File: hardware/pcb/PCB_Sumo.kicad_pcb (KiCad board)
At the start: 2 copper layers, 60 x 80 mm, 31 parts

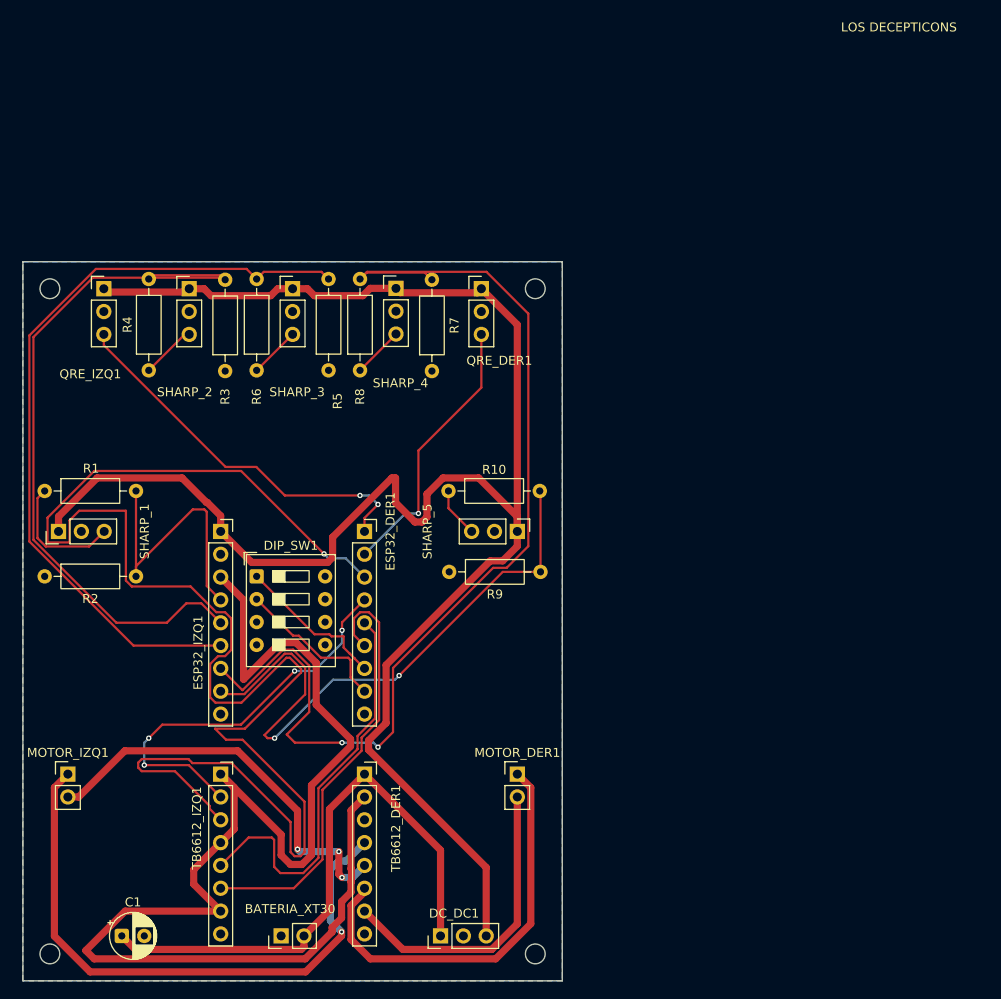
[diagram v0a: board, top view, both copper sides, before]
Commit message: PCB v2 (WIP): divisor de batería en GP6, ESP32 a 15.24 mm
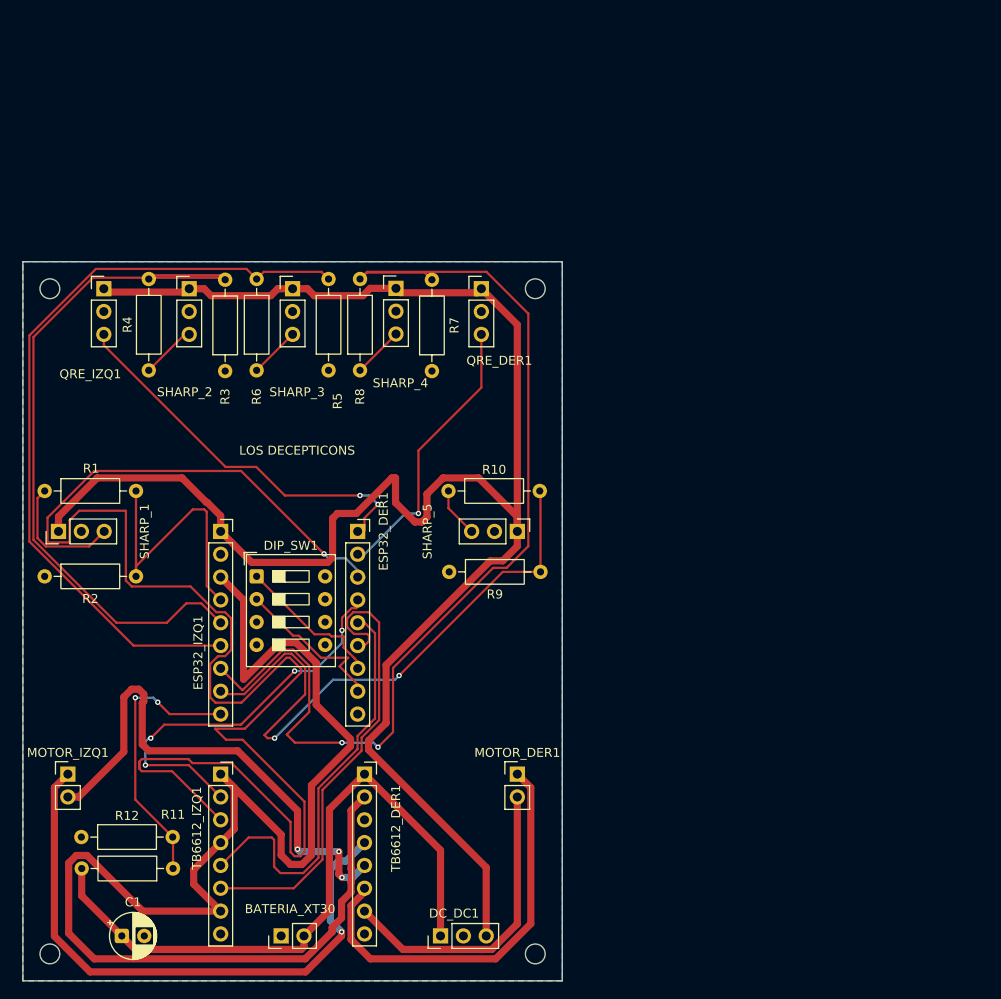
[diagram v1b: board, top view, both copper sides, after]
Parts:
- added R11: 20k, Resistor_THT:R_Axial_DIN0207_L6.3mm_D2.5mm_P10.16mm_Horizontal, F.Cu at (130.7, 132.5)
- added R12: 10k, Resistor_THT:R_Axial_DIN0207_L6.3mm_D2.5mm_P10.16mm_Horizontal, F.Cu at (120.5, 129.0)
- moved ESP32_DER1 0.76 mm to (151.2, 95.0)
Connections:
- ESP32_IZQ1 pad 9: unconnected-(ESP32_IZQ1-Pin_9-Pad9) -> /V_BAT_SENSE
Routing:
- net /V_BAT_SENSE: track 0.00 -> 31.0 mm, vias 0 -> 2
- net +3.3V: track 145.3 -> 158.8 mm
- net /MOT_A2: track 45.5 -> 58.3 mm
- net /+7.4V: track 64.5 -> 73.9 mm
- net /BIN2: track 48.7 -> 51.1 mm
- net +5V: track 205.9 -> 207.2 mm
- net /SW_2: track 17.4 -> 18.2 mm
